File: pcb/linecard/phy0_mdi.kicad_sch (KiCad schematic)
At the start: 99 parts, among them J2 LPJG47036AWNL, J5 LPJG47036AWNL, U10 VSC8512, U11 ESD224DQAR, U12 ESD224DQAR, U13 ESD224DQAR, U14 ESD224DQAR, U15 ESD224DQAR, U16 ESD224DQAR, U17 ESD224DQAR, U18 ESD224DQAR, U19 ESD224DQAR, U20 ESD224DQAR, U21 ESD224DQAR, U22 ESD224DQAR, U23 ESD224DQAR, U24 ESD224DQAR, U25 ESD224DQAR, U26 ESD224DQAR, U27 ESD224DQAR, U28 ESD224DQAR, U29 ESD224DQAR, U30 ESD224DQAR, U31 ESD224DQAR, U32 ESD224DQAR, U33 ESD224DQAR, U34 ESD224DQAR

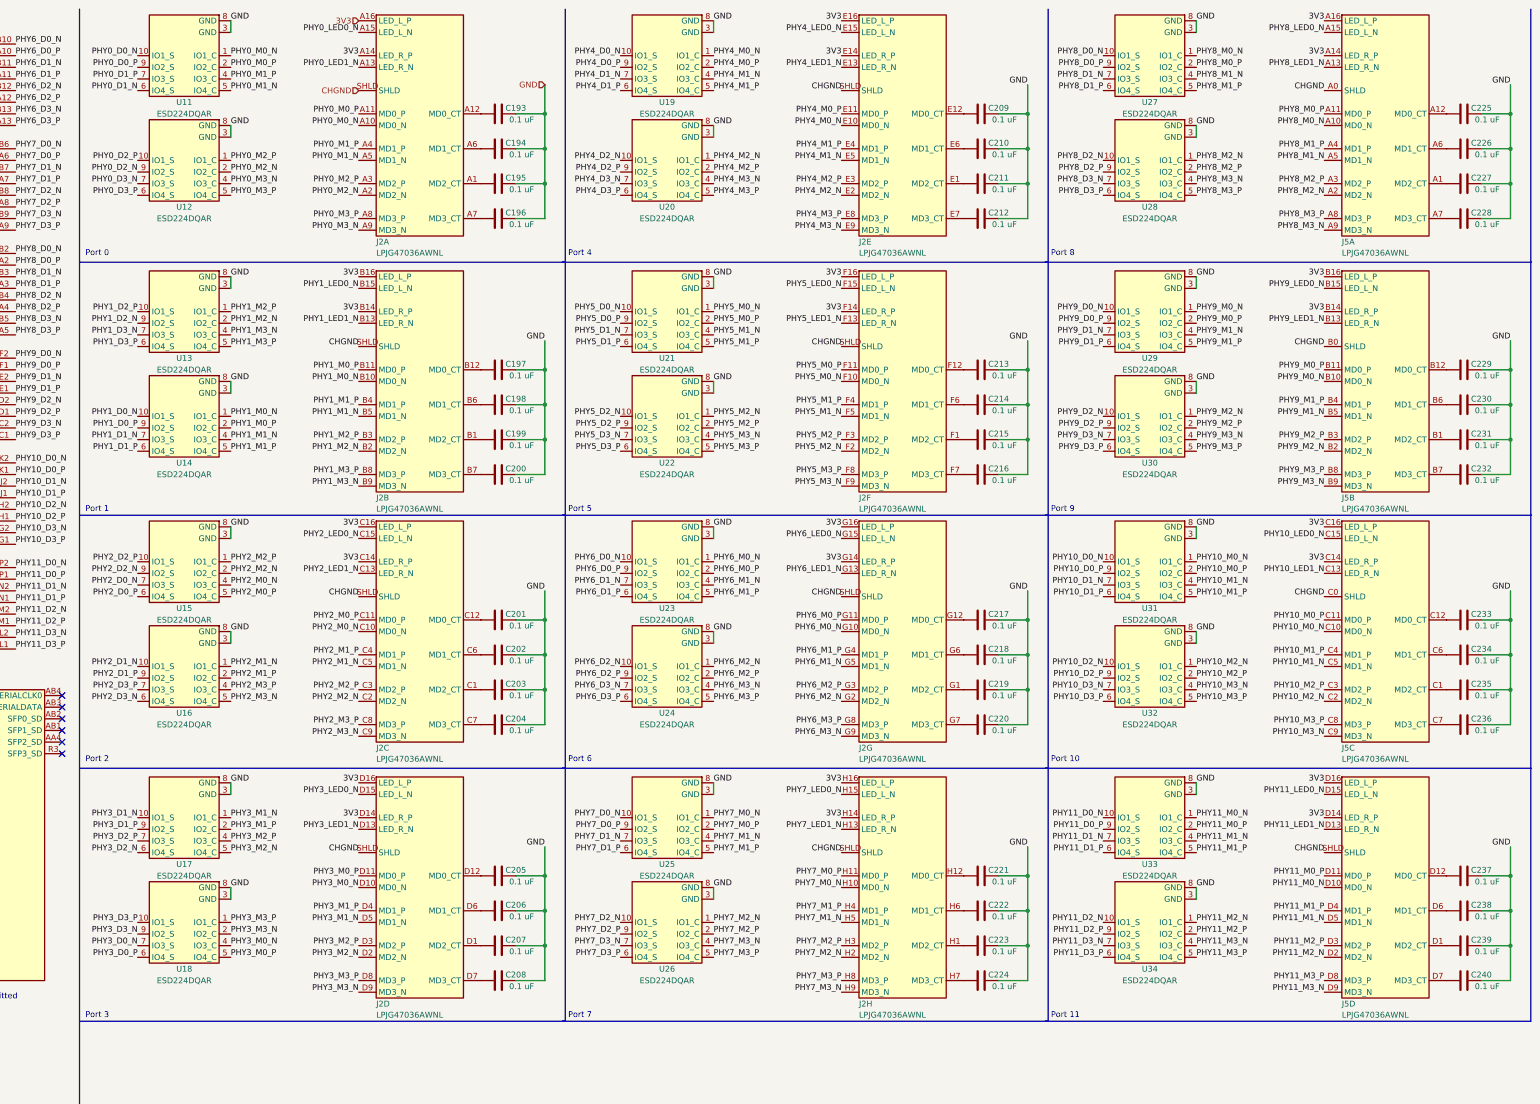
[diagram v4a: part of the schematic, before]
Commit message: COntinued routing baseT pairs on left PHY
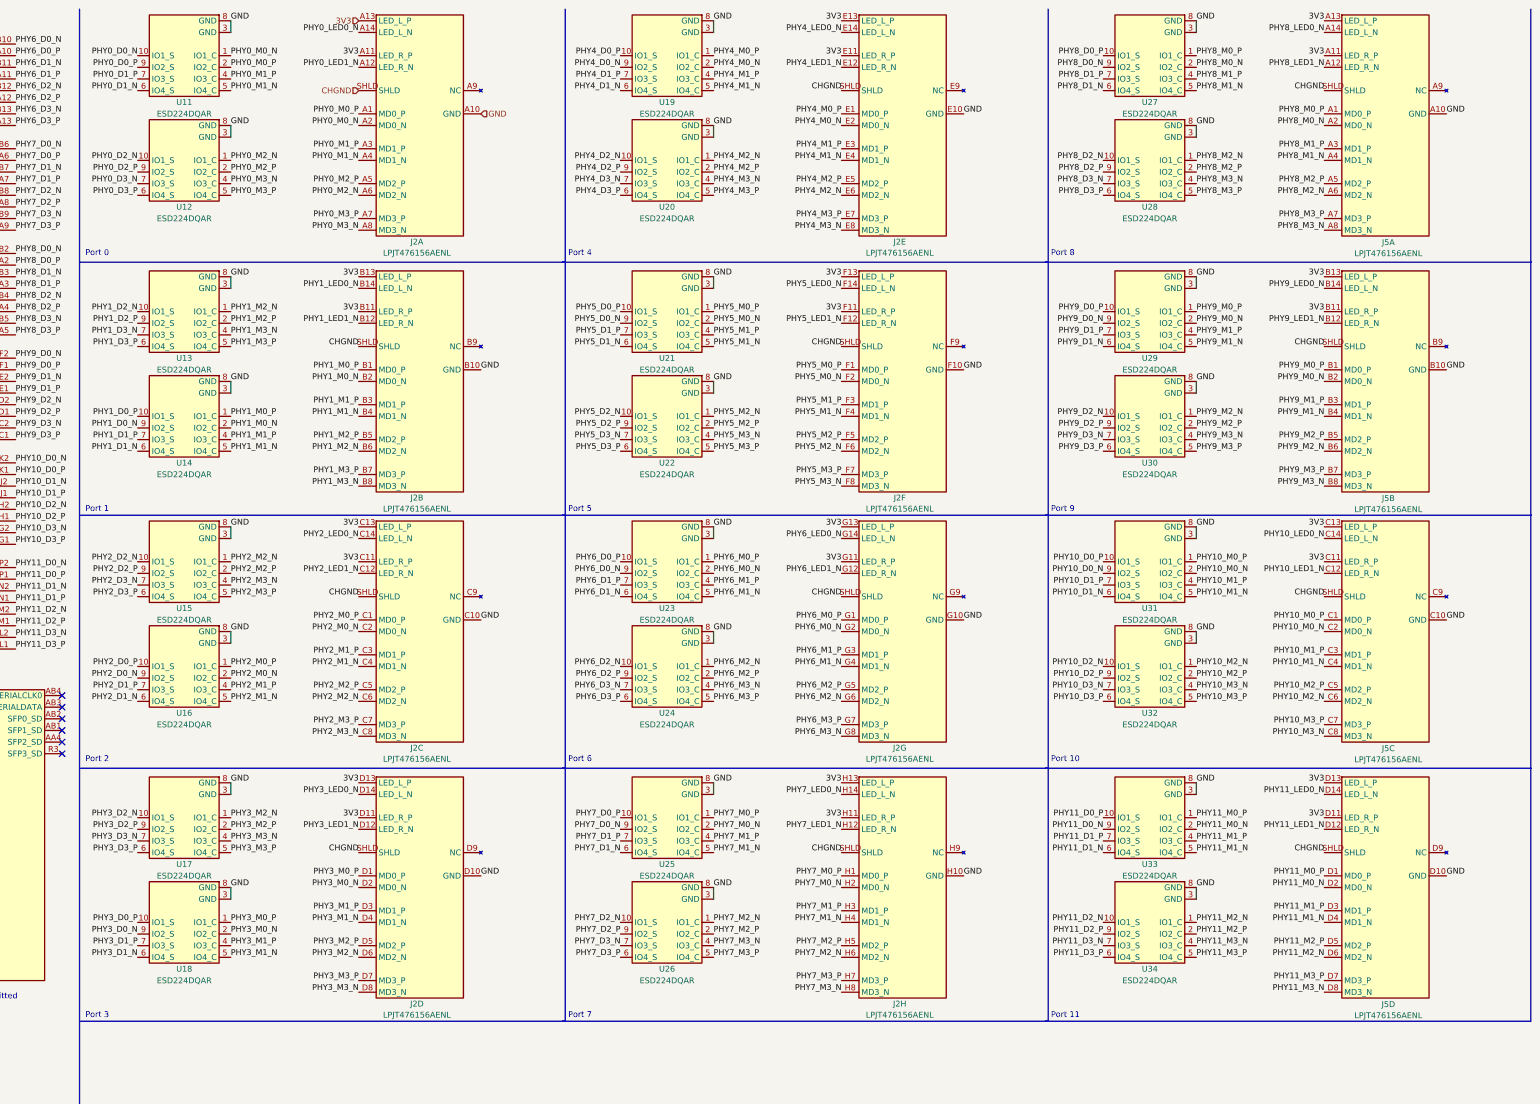
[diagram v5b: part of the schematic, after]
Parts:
- removed C193, C194, C195, C196, C197, C198, C199, C200, C201, C202, C203, C204, C205, C206, C207, C208, C209, C210, C211, C212, C213, C214, C215, C216, C217, C218, C219, C220, C221, C222, C223, C224, C225, C226, C227, C228, C229, C230, C231, C232, C233, C234, C235, C236, C237, C238, C239, C240: 0.1 uF, azonenberg_pcb:EIA_0402_CAP_NOSILK, symbol device:C
- removed J2, J5: LPJG47036AWNL, azonenberg_pcb:CONN_LINKPP_LPJG47036AWNL, symbol special-azonenberg:LPJG47036AWNL
- added J2, J5: LPJT476156AENL, azonenberg_pcb:CONN_LINKPP_LPJT476156AENL, symbol special-azonenberg:LPJT476156AENL
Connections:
- net 3V3: now also J2.A11 (LED_R_P), J2.A13 (LED_L_P), J2.B11 (LED_R_P), J2.B13 (LED_L_P), J2.C11 (LED_R_P), J2.C13 (LED_L_P), J2.D11 (LED_R_P), J2.D13 (LED_L_P), J2.E11 (LED_R_P), J2.E13 (LED_L_P), J2.F11 (LED_R_P), J2.F13 (LED_L_P), J2.G11 (LED_R_P), J2.G13 (LED_L_P), J2.H11 (LED_R_P), J2.H13 (LED_L_P), J5.A11 (LED_R_P), J5.A13 (LED_L_P), J5.B11 (LED_R_P), J5.B13 (LED_L_P), J5.C11 (LED_R_P), J5.C13 (LED_L_P), J5.D11 (LED_R_P), J5.D13 (LED_L_P)
- net CHGND: now also J2.SHLD, J2.SHLD, J2.SHLD, J2.SHLD, J2.SHLD, J2.SHLD, J2.SHLD, J2.SHLD, J5.SHLD, J5.SHLD, J5.SHLD, J5.SHLD
- net GND: now also J2.A10 (GND), J2.B10 (GND), J2.C10 (GND), J2.D10 (GND), J2.E10 (GND), J2.F10 (GND), J2.G10 (GND), J2.H10 (GND), J5.A10 (GND), J5.B10 (GND), J5.C10 (GND), J5.D10 (GND)
- net PHY0_D2_N: now also U12.10 (IO1_S); no longer U12.9 (IO2_S)
- net PHY0_D2_P: now also U12.9 (IO2_S); no longer U12.10 (IO1_S)
- net PHY0_LED0_N: now also J2.A14 (LED_L_N)
- net PHY0_LED1_N: now also J2.A12 (LED_R_N)
- net PHY0_M0_N: now also J2.A2 (MD0_N)
- net PHY0_M0_P: now also J2.A1 (MD0_P)
- net PHY0_M1_N: now also J2.A4 (MD1_N)
- net PHY0_M1_P: now also J2.A3 (MD1_P)
- net PHY0_M2_N: now also U12.1 (IO1_C), J2.A6 (MD2_N); no longer U12.2 (IO2_C)
- net PHY0_M2_P: now also U12.2 (IO2_C), J2.A5 (MD2_P); no longer U12.1 (IO1_C)
- net PHY0_M3_N: now also J2.A8 (MD3_N)
- net PHY0_M3_P: now also J2.A7 (MD3_P)
- net PHY10_D0_N: now also U31.9 (IO2_S); no longer U31.10 (IO1_S)
- net PHY10_D0_P: now also U31.10 (IO1_S); no longer U31.9 (IO2_S)
- net PHY10_D1_N: now also U31.6 (IO4_S); no longer U31.7 (IO3_S)
- net PHY10_D1_P: now also U31.7 (IO3_S); no longer U31.6 (IO4_S)
- net PHY10_LED0_N: now also J5.C14 (LED_L_N)
- net PHY10_LED1_N: now also J5.C12 (LED_R_N)
- net PHY10_M0_N: now also U31.2 (IO2_C), J5.C2 (MD0_N); no longer U31.1 (IO1_C)
- net PHY10_M0_P: now also U31.1 (IO1_C), J5.C1 (MD0_P); no longer U31.2 (IO2_C)
- net PHY10_M1_N: now also U31.5 (IO4_C), J5.C4 (MD1_N); no longer U31.4 (IO3_C)
- net PHY10_M1_P: now also U31.4 (IO3_C), J5.C3 (MD1_P); no longer U31.5 (IO4_C)
- net PHY10_M2_N: now also J5.C6 (MD2_N)
- net PHY10_M2_P: now also J5.C5 (MD2_P)
- net PHY10_M3_N: now also J5.C8 (MD3_N)
- net PHY10_M3_P: now also J5.C7 (MD3_P)
- net PHY11_D0_N: now also U33.9 (IO2_S); no longer U33.10 (IO1_S)
- net PHY11_D0_P: now also U33.10 (IO1_S); no longer U33.9 (IO2_S)
- net PHY11_D1_N: now also U33.6 (IO4_S); no longer U33.7 (IO3_S)
- net PHY11_D1_P: now also U33.7 (IO3_S); no longer U33.6 (IO4_S)
- net PHY11_LED0_N: now also J5.D14 (LED_L_N)
- net PHY11_LED1_N: now also J5.D12 (LED_R_N)
- net PHY11_M0_N: now also U33.2 (IO2_C), J5.D2 (MD0_N); no longer U33.1 (IO1_C)
- net PHY11_M0_P: now also U33.1 (IO1_C), J5.D1 (MD0_P); no longer U33.2 (IO2_C)
- net PHY11_M1_N: now also U33.5 (IO4_C), J5.D4 (MD1_N); no longer U33.4 (IO3_C)
- net PHY11_M1_P: now also U33.4 (IO3_C), J5.D3 (MD1_P); no longer U33.5 (IO4_C)
- net PHY11_M2_N: now also J5.D6 (MD2_N)
- net PHY11_M2_P: now also J5.D5 (MD2_P)
- net PHY11_M3_N: now also J5.D8 (MD3_N)
- net PHY11_M3_P: now also J5.D7 (MD3_P)
- net PHY1_D0_N: now also U14.9 (IO2_S); no longer U14.10 (IO1_S)
- net PHY1_D0_P: now also U14.10 (IO1_S); no longer U14.9 (IO2_S)
- net PHY1_D1_N: now also U14.6 (IO4_S); no longer U14.7 (IO3_S)
- net PHY1_D1_P: now also U14.7 (IO3_S); no longer U14.6 (IO4_S)
- net PHY1_D2_N: now also U13.10 (IO1_S); no longer U13.9 (IO2_S)
- net PHY1_D2_P: now also U13.9 (IO2_S); no longer U13.10 (IO1_S)
- net PHY1_LED0_N: now also J2.B14 (LED_L_N)
- net PHY1_LED1_N: now also J2.B12 (LED_R_N)
- net PHY1_M0_N: now also U14.2 (IO2_C), J2.B2 (MD0_N); no longer U14.1 (IO1_C)
- net PHY1_M0_P: now also U14.1 (IO1_C), J2.B1 (MD0_P); no longer U14.2 (IO2_C)
- net PHY1_M1_N: now also U14.5 (IO4_C), J2.B4 (MD1_N); no longer U14.4 (IO3_C)
- net PHY1_M1_P: now also U14.4 (IO3_C), J2.B3 (MD1_P); no longer U14.5 (IO4_C)
- net PHY1_M2_N: now also U13.1 (IO1_C), J2.B6 (MD2_N); no longer U13.2 (IO2_C)
- net PHY1_M2_P: now also U13.2 (IO2_C), J2.B5 (MD2_P); no longer U13.1 (IO1_C)
- net PHY1_M3_N: now also J2.B8 (MD3_N)
- net PHY1_M3_P: now also J2.B7 (MD3_P)
- net PHY2_D0_N: now also U16.9 (IO2_S); no longer U15.7 (IO3_S)
- net PHY2_D0_P: now also U16.10 (IO1_S); no longer U15.6 (IO4_S)
- net PHY2_D1_N: now also U16.6 (IO4_S); no longer U16.10 (IO1_S)
- net PHY2_D1_P: now also U16.7 (IO3_S); no longer U16.9 (IO2_S)
- net PHY2_D2_N: now also U15.10 (IO1_S); no longer U15.9 (IO2_S)
- net PHY2_D2_P: now also U15.9 (IO2_S); no longer U15.10 (IO1_S)
- net PHY2_D3_N: now also U15.7 (IO3_S); no longer U16.6 (IO4_S)
- net PHY2_D3_P: now also U15.6 (IO4_S); no longer U16.7 (IO3_S)
- net PHY2_LED0_N: now also J2.C14 (LED_L_N)
- net PHY2_LED1_N: now also J2.C12 (LED_R_N)
- net PHY2_M0_N: now also U16.2 (IO2_C), J2.C2 (MD0_N); no longer U15.4 (IO3_C)
- net PHY2_M0_P: now also U16.1 (IO1_C), J2.C1 (MD0_P); no longer U15.5 (IO4_C)
- net PHY2_M1_N: now also U16.5 (IO4_C), J2.C4 (MD1_N); no longer U16.1 (IO1_C)
- net PHY2_M1_P: now also U16.4 (IO3_C), J2.C3 (MD1_P); no longer U16.2 (IO2_C)
- net PHY2_M2_N: now also U15.1 (IO1_C), J2.C6 (MD2_N); no longer U15.2 (IO2_C)
- net PHY2_M2_P: now also U15.2 (IO2_C), J2.C5 (MD2_P); no longer U15.1 (IO1_C)
- net PHY2_M3_N: now also U15.4 (IO3_C), J2.C8 (MD3_N); no longer U16.5 (IO4_C)
- net PHY2_M3_P: now also U15.5 (IO4_C), J2.C7 (MD3_P); no longer U16.4 (IO3_C)
- net PHY3_D0_N: now also U18.9 (IO2_S); no longer U18.7 (IO3_S)
- net PHY3_D0_P: now also U18.10 (IO1_S); no longer U18.6 (IO4_S)
- net PHY3_D1_N: now also U18.6 (IO4_S); no longer U17.10 (IO1_S)
- net PHY3_D1_P: now also U18.7 (IO3_S); no longer U17.9 (IO2_S)
- net PHY3_D2_N: now also U17.10 (IO1_S); no longer U17.6 (IO4_S)
- net PHY3_D2_P: now also U17.9 (IO2_S); no longer U17.7 (IO3_S)
- net PHY3_D3_N: now also U17.7 (IO3_S); no longer U18.9 (IO2_S)
- net PHY3_D3_P: now also U17.6 (IO4_S); no longer U18.10 (IO1_S)
- net PHY3_LED0_N: now also J2.D14 (LED_L_N)
- net PHY3_LED1_N: now also J2.D12 (LED_R_N)
- net PHY3_M0_N: now also U18.2 (IO2_C), J2.D2 (MD0_N); no longer U18.4 (IO3_C)
- net PHY3_M0_P: now also U18.1 (IO1_C), J2.D1 (MD0_P); no longer U18.5 (IO4_C)
- net PHY3_M1_N: now also U18.5 (IO4_C), J2.D4 (MD1_N); no longer U17.1 (IO1_C)
- net PHY3_M1_P: now also U18.4 (IO3_C), J2.D3 (MD1_P); no longer U17.2 (IO2_C)
- net PHY3_M2_N: now also U17.1 (IO1_C), J2.D6 (MD2_N); no longer U17.5 (IO4_C)
- net PHY3_M2_P: now also U17.2 (IO2_C), J2.D5 (MD2_P); no longer U17.4 (IO3_C)
- net PHY3_M3_N: now also U17.4 (IO3_C), J2.D8 (MD3_N); no longer U18.2 (IO2_C)
- net PHY3_M3_P: now also U17.5 (IO4_C), J2.D7 (MD3_P); no longer U18.1 (IO1_C)
- net PHY4_D0_N: now also U19.9 (IO2_S); no longer U19.10 (IO1_S)
- net PHY4_D0_P: now also U19.10 (IO1_S); no longer U19.9 (IO2_S)
- net PHY4_D1_N: now also U19.6 (IO4_S); no longer U19.7 (IO3_S)
- net PHY4_D1_P: now also U19.7 (IO3_S); no longer U19.6 (IO4_S)
- net PHY4_LED0_N: now also J2.E14 (LED_L_N)
- net PHY4_LED1_N: now also J2.E12 (LED_R_N)
- net PHY4_M0_N: now also U19.2 (IO2_C), J2.E2 (MD0_N); no longer U19.1 (IO1_C)
- net PHY4_M0_P: now also U19.1 (IO1_C), J2.E1 (MD0_P); no longer U19.2 (IO2_C)
- net PHY4_M1_N: now also U19.5 (IO4_C), J2.E4 (MD1_N); no longer U19.4 (IO3_C)
- net PHY4_M1_P: now also U19.4 (IO3_C), J2.E3 (MD1_P); no longer U19.5 (IO4_C)
- net PHY4_M2_N: now also J2.E6 (MD2_N)
- net PHY4_M2_P: now also J2.E5 (MD2_P)
- net PHY4_M3_N: now also J2.E8 (MD3_N)
- net PHY4_M3_P: now also J2.E7 (MD3_P)
- net PHY5_D0_N: now also U21.9 (IO2_S); no longer U21.10 (IO1_S)
- net PHY5_D0_P: now also U21.10 (IO1_S); no longer U21.9 (IO2_S)
- net PHY5_D1_N: now also U21.6 (IO4_S); no longer U21.7 (IO3_S)
- net PHY5_D1_P: now also U21.7 (IO3_S); no longer U21.6 (IO4_S)
- net PHY5_LED0_N: now also J2.F14 (LED_L_N)
- net PHY5_LED1_N: now also J2.F12 (LED_R_N)
- net PHY5_M0_N: now also U21.2 (IO2_C), J2.F2 (MD0_N); no longer U21.1 (IO1_C)
- net PHY5_M0_P: now also U21.1 (IO1_C), J2.F1 (MD0_P); no longer U21.2 (IO2_C)
- net PHY5_M1_N: now also U21.5 (IO4_C), J2.F4 (MD1_N); no longer U21.4 (IO3_C)
- net PHY5_M1_P: now also U21.4 (IO3_C), J2.F3 (MD1_P); no longer U21.5 (IO4_C)
- net PHY5_M2_N: now also J2.F6 (MD2_N)
- net PHY5_M2_P: now also J2.F5 (MD2_P)
- net PHY5_M3_N: now also J2.F8 (MD3_N)
- net PHY5_M3_P: now also J2.F7 (MD3_P)
- net PHY6_D0_N: now also U23.9 (IO2_S); no longer U23.10 (IO1_S)
- net PHY6_D0_P: now also U23.10 (IO1_S); no longer U23.9 (IO2_S)
- net PHY6_D1_N: now also U23.6 (IO4_S); no longer U23.7 (IO3_S)
- net PHY6_D1_P: now also U23.7 (IO3_S); no longer U23.6 (IO4_S)
- net PHY6_LED0_N: now also J2.G14 (LED_L_N)
- net PHY6_LED1_N: now also J2.G12 (LED_R_N)
- net PHY6_M0_N: now also U23.2 (IO2_C), J2.G2 (MD0_N); no longer U23.1 (IO1_C)
- net PHY6_M0_P: now also U23.1 (IO1_C), J2.G1 (MD0_P); no longer U23.2 (IO2_C)
- net PHY6_M1_N: now also U23.5 (IO4_C), J2.G4 (MD1_N); no longer U23.4 (IO3_C)
- net PHY6_M1_P: now also U23.4 (IO3_C), J2.G3 (MD1_P); no longer U23.5 (IO4_C)
- net PHY6_M2_N: now also J2.G6 (MD2_N)
- net PHY6_M2_P: now also J2.G5 (MD2_P)
- net PHY6_M3_N: now also J2.G8 (MD3_N)
- net PHY6_M3_P: now also J2.G7 (MD3_P)
- net PHY7_D0_N: now also U25.9 (IO2_S); no longer U25.10 (IO1_S)
- net PHY7_D0_P: now also U25.10 (IO1_S); no longer U25.9 (IO2_S)
- net PHY7_D1_N: now also U25.6 (IO4_S); no longer U25.7 (IO3_S)
- net PHY7_D1_P: now also U25.7 (IO3_S); no longer U25.6 (IO4_S)
- net PHY7_LED0_N: now also J2.H14 (LED_L_N)
- net PHY7_LED1_N: now also J2.H12 (LED_R_N)
- net PHY7_M0_N: now also U25.2 (IO2_C), J2.H2 (MD0_N); no longer U25.1 (IO1_C)
- net PHY7_M0_P: now also U25.1 (IO1_C), J2.H1 (MD0_P); no longer U25.2 (IO2_C)
- net PHY7_M1_N: now also U25.5 (IO4_C), J2.H4 (MD1_N); no longer U25.4 (IO3_C)
- net PHY7_M1_P: now also U25.4 (IO3_C), J2.H3 (MD1_P); no longer U25.5 (IO4_C)
- net PHY7_M2_N: now also J2.H6 (MD2_N)
- net PHY7_M2_P: now also J2.H5 (MD2_P)
- net PHY7_M3_N: now also J2.H8 (MD3_N)
- net PHY7_M3_P: now also J2.H7 (MD3_P)
- net PHY8_D0_N: now also U27.9 (IO2_S); no longer U27.10 (IO1_S)
- net PHY8_D0_P: now also U27.10 (IO1_S); no longer U27.9 (IO2_S)
- net PHY8_D1_N: now also U27.6 (IO4_S); no longer U27.7 (IO3_S)
- net PHY8_D1_P: now also U27.7 (IO3_S); no longer U27.6 (IO4_S)
- net PHY8_LED0_N: now also J5.A14 (LED_L_N)
- net PHY8_LED1_N: now also J5.A12 (LED_R_N)
- net PHY8_M0_N: now also U27.2 (IO2_C), J5.A2 (MD0_N); no longer U27.1 (IO1_C)
- net PHY8_M0_P: now also U27.1 (IO1_C), J5.A1 (MD0_P); no longer U27.2 (IO2_C)
- net PHY8_M1_N: now also U27.5 (IO4_C), J5.A4 (MD1_N); no longer U27.4 (IO3_C)
- net PHY8_M1_P: now also U27.4 (IO3_C), J5.A3 (MD1_P); no longer U27.5 (IO4_C)
- net PHY8_M2_N: now also J5.A6 (MD2_N)
- net PHY8_M2_P: now also J5.A5 (MD2_P)
- net PHY8_M3_N: now also J5.A8 (MD3_N)
- net PHY8_M3_P: now also J5.A7 (MD3_P)
- net PHY9_D0_N: now also U29.9 (IO2_S); no longer U29.10 (IO1_S)
- net PHY9_D0_P: now also U29.10 (IO1_S); no longer U29.9 (IO2_S)
- net PHY9_D1_N: now also U29.6 (IO4_S); no longer U29.7 (IO3_S)
- net PHY9_D1_P: now also U29.7 (IO3_S); no longer U29.6 (IO4_S)
- net PHY9_LED0_N: now also J5.B14 (LED_L_N)
- net PHY9_LED1_N: now also J5.B12 (LED_R_N)
- net PHY9_M0_N: now also U29.2 (IO2_C), J5.B2 (MD0_N); no longer U29.1 (IO1_C)
- net PHY9_M0_P: now also U29.1 (IO1_C), J5.B1 (MD0_P); no longer U29.2 (IO2_C)
- net PHY9_M1_N: now also U29.5 (IO4_C), J5.B4 (MD1_N); no longer U29.4 (IO3_C)
- net PHY9_M1_P: now also U29.4 (IO3_C), J5.B3 (MD1_P); no longer U29.5 (IO4_C)
- net PHY9_M2_N: now also J5.B6 (MD2_N)
- net PHY9_M2_P: now also J5.B5 (MD2_P)
- net PHY9_M3_N: now also J5.B8 (MD3_N)
- net PHY9_M3_P: now also J5.B7 (MD3_P)
